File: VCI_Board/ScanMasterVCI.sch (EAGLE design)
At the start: 64 parts, among them IC1 XMEGA16A4A, IC2 LTC3631, IC3 LM317MDT, IC4 SN74AHCT1G04, IC5 SN74AHCT1G04, IC6 TL331, IC7 74AHCT1G32DBV, Q5 PZT3904, Q6 MMBT3904, Q7 MMBT4403, Q8 MMBT3904/SOT, U2 LM339MA, U3 MAX17502EATB+T, U4 MAX13444EASA+

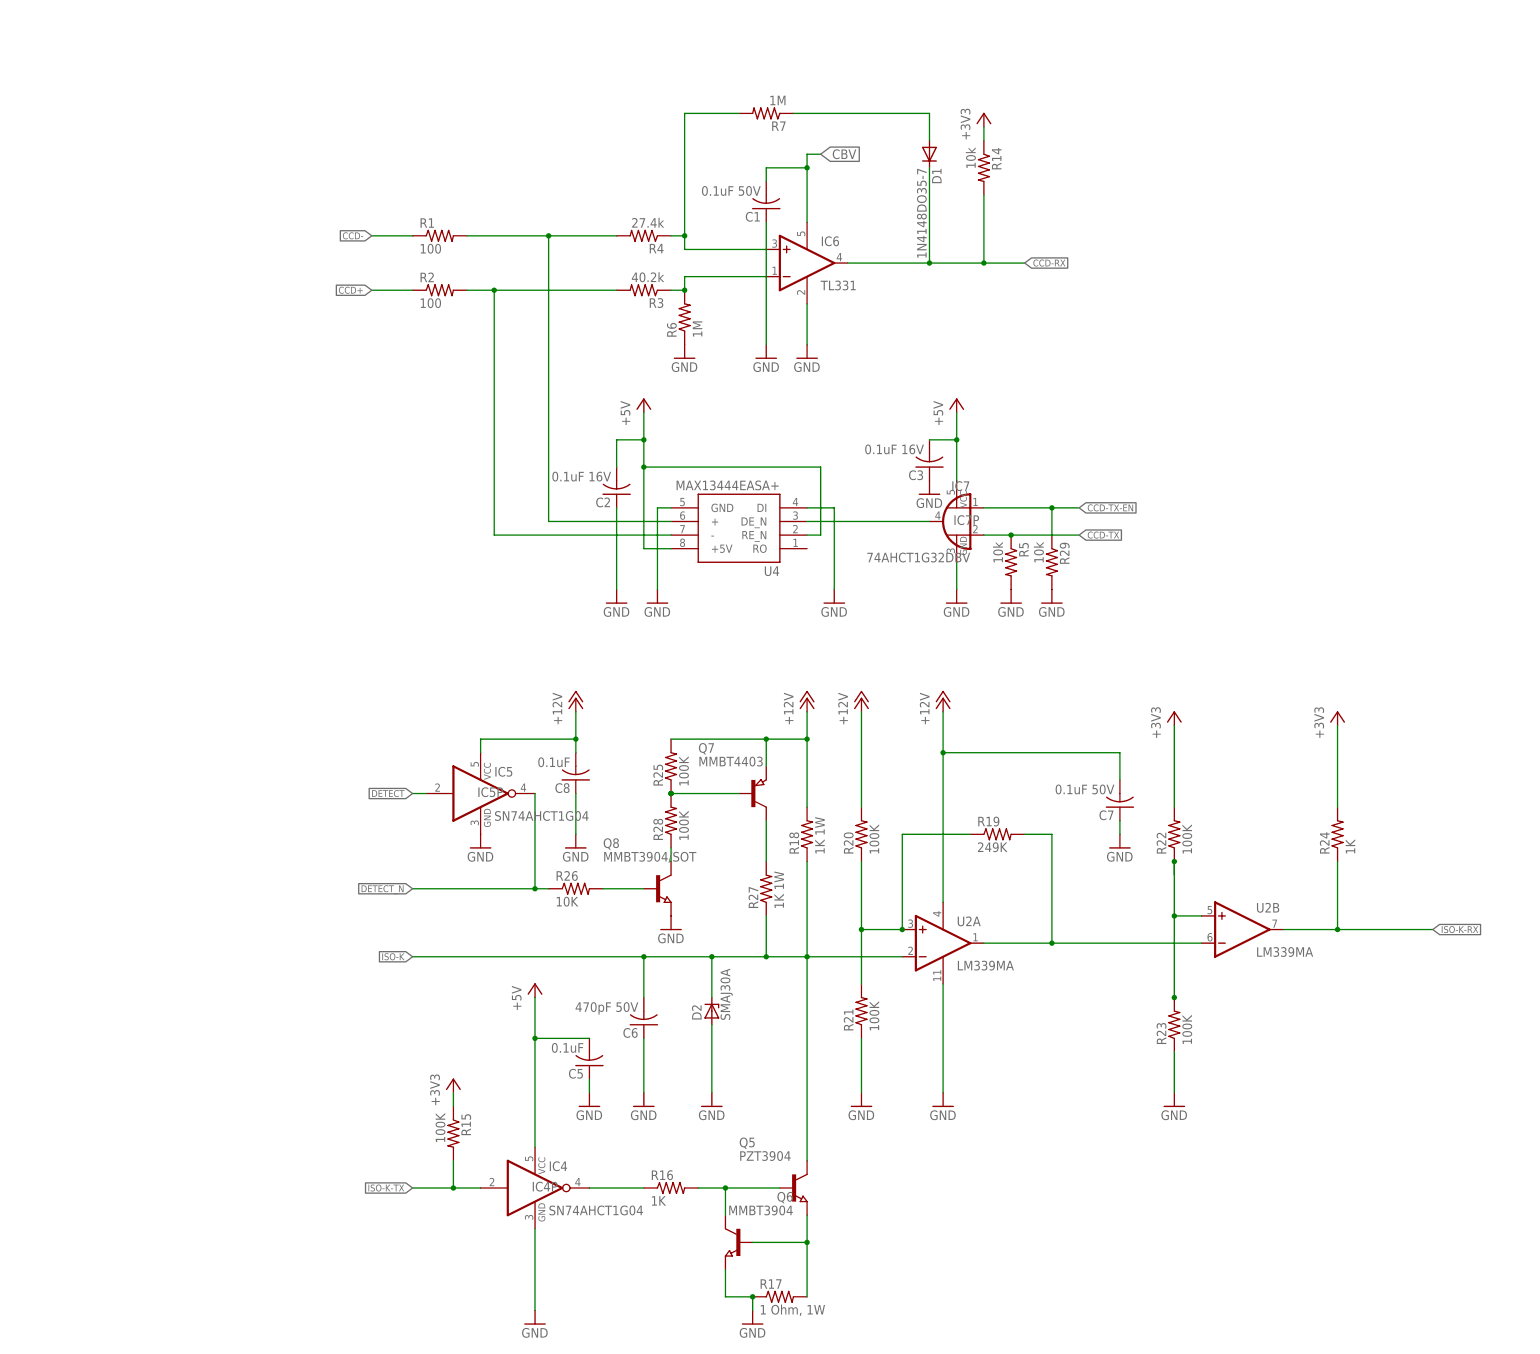
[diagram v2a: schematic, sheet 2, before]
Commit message: Designed a circuit for J1850VPW. Still some problems to be worked out, I think the input voltage is all wrong, but I'll need to put a scope on some J1850 ECU's to see exactly what my target "high" voltage should be.
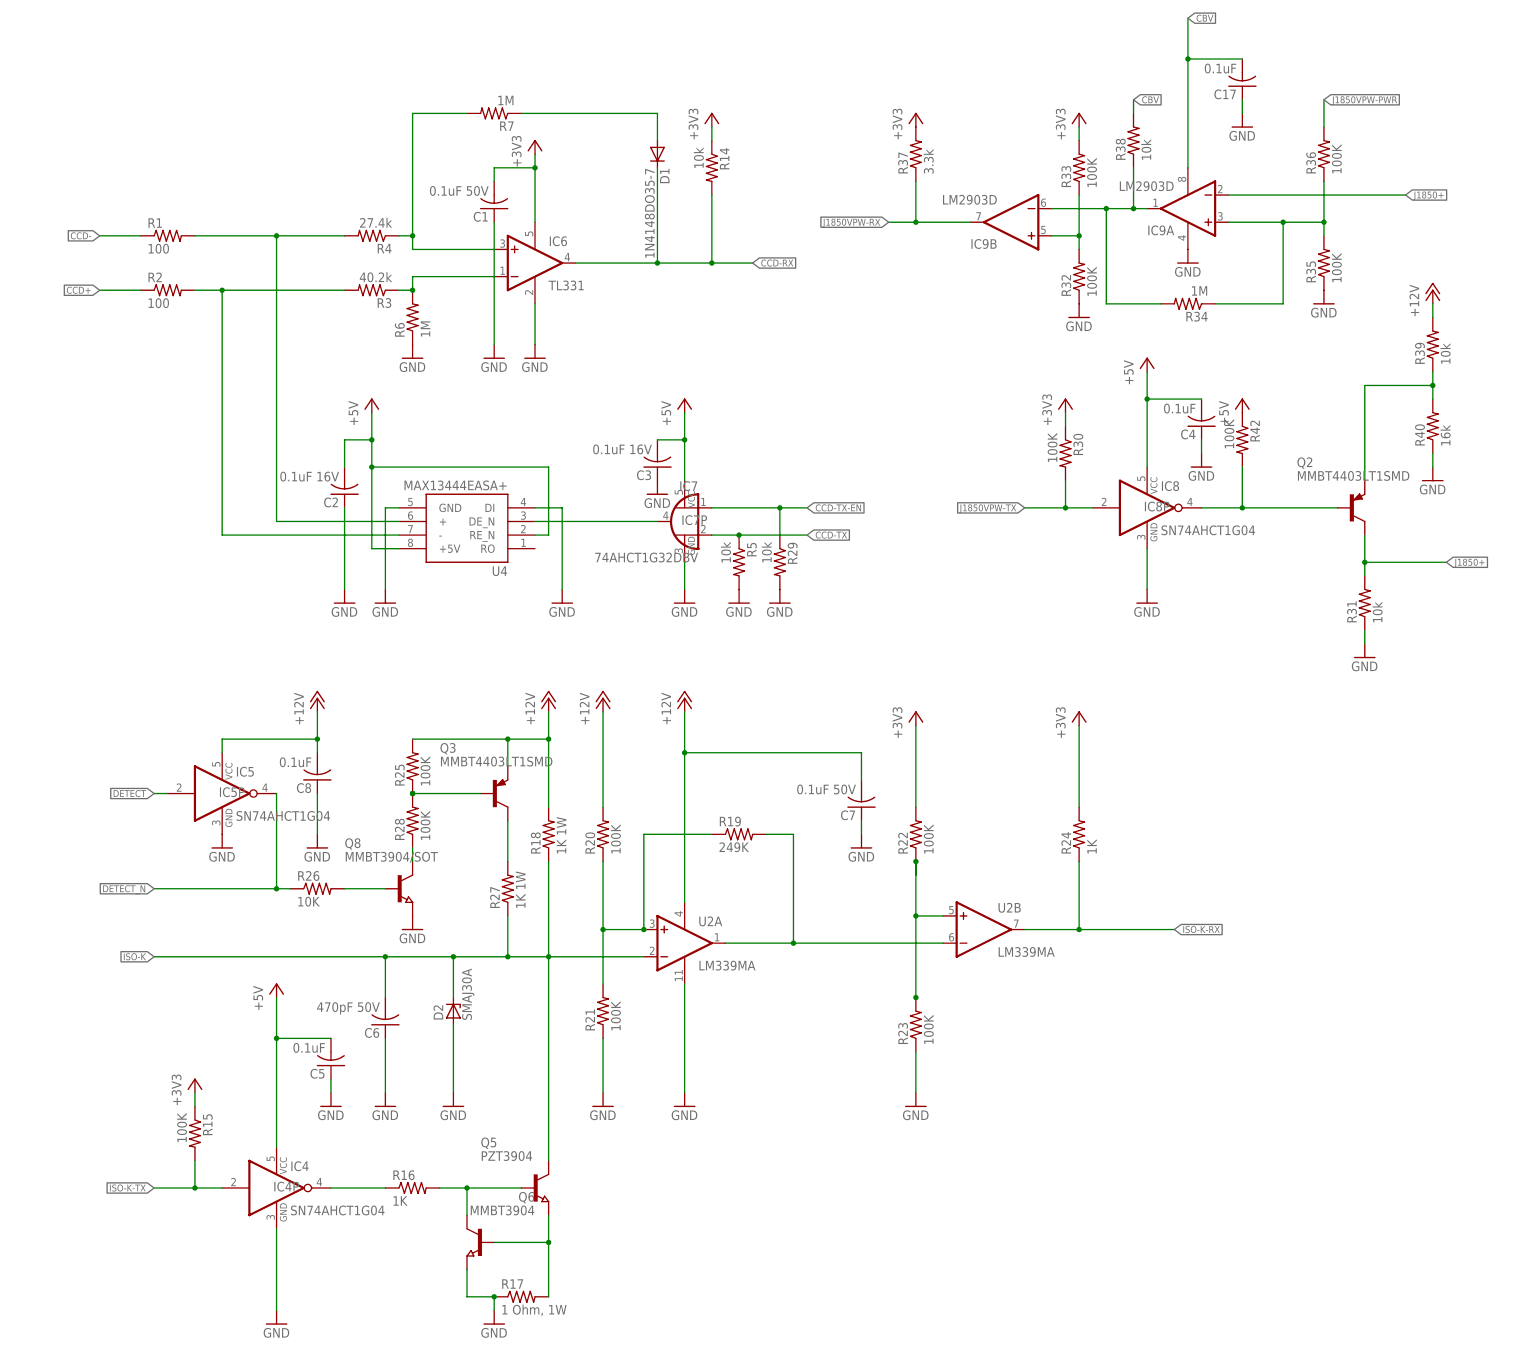
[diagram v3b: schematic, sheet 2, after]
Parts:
- removed Q7: MMBT4403, semicon-smd-ipc:PNP-TRANSISTOR_SOT23
- added C17, C4: 0.1uF, adafruit:C-USC0805
- added IC8: SN74AHCT1G04, 74xx-little-us:74AHC1G04DBV
- added IC9: LM2903D, linear:LM2903D
- added Q2, Q3: MMBT4403LT1SMD, transistor-pnp:MMBT4403LT1SMD
- added R30, R32, R33, R35, R36, R42: 100K, adafruit:R-US_R0805W
- added R31, R38, R39: 10k, adafruit:R-US_R0805W
- added R34: 1M, adafruit:R-US_R0805W
- added R37: 3.3k, adafruit:R-US_R0805W
- added R40: 16k, adafruit:R-US_R0805W
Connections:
- new net J1850+: IC9A.-IN, Q2.C, R31.2
- new net J1850VPW-RX: IC9B.OUT, R37.1
- new net J1850VPW-TX: IC8A.I, R30.2
- new net N$25: Q2.E, R39.1, R40.2
- new net N$27: IC9A.OUT, IC9B.-IN, R34.2, R38.1
- new net N$28: IC9B.+IN, R32.2, R33.1
- new net N$29: IC9A.+IN, R34.1, R35.2
- new net N$5: IC8A.O, Q2.B, R42.2
- net +12V: now also Q3.E, R39.2; no longer Q7.E
- net +3V3: now also C1.2, IC6.V+, R30.1, R33.2, R37.2
- net +5V: now also C4.2, IC8P.VCC, R42.1
- net CBV: now also C17.2, IC9P.V+, R38.2; no longer C1.2, IC6.V+
- net GND: now also C17.1, C4.1, IC8P.GND, IC9P.V-, R31.1, R32.1, R40.1
- net J1850VPW-PWR: now also R36.2
- net N$20: now also Q3.B; no longer Q7.B
- net N$23: now also Q3.C; no longer Q7.C
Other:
- moved on the sheet: C1, C2, C3, C5, C6, C7, C8, D1, D2, IC4, IC4P, IC5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

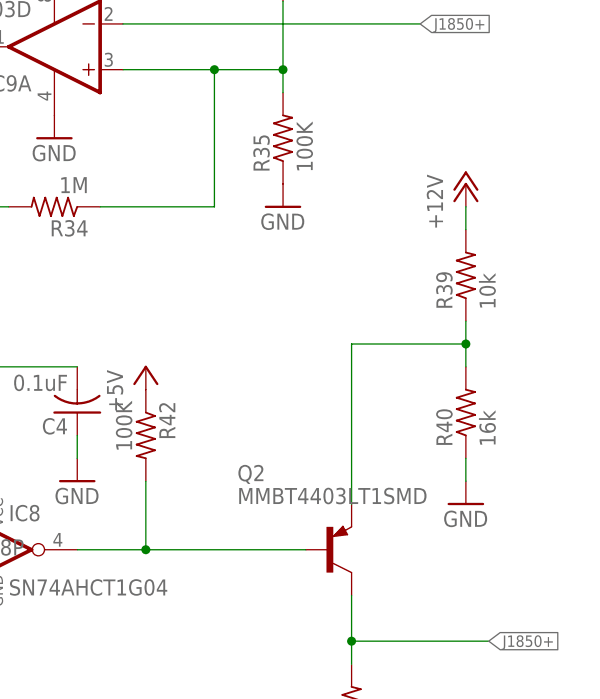
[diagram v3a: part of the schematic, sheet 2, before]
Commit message: Modified J1850 based on power findings
Scope shows ~7.3V for high signals. Unsure if current RX circuit is sufficient to drive that down to 3.3 volts. Still looking into more elegant solution.
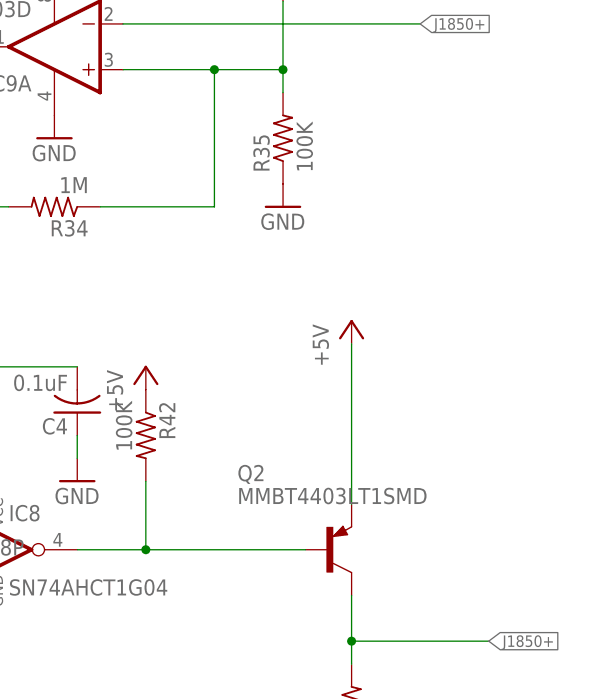
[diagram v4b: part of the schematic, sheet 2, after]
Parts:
- removed R39: 10k, adafruit:R-US_R0805W
- removed R40: 16k, adafruit:R-US_R0805W
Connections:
- removed net N$25: Q2.E, R39.1, R40.2
- net +12V: no longer R39.2
- net +5V: now also Q2.E
- net GND: no longer R40.1
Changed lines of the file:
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@@
 <part name="R31" library="adafruit" library_urn="urn:adsk.eagle:library:420" deviceset="R-US_" device="R0805W" value="10k"/>
 <part name="+3V10" library="supply1" library_urn="urn:adsk.eagle:library:371" deviceset="+3V3" device=""/>
-<part name="P+12" library="supply1" library_urn="urn:adsk.eagle:library:371" deviceset="+12V" device=""/>
-<part name="R39" library="adafruit" library_urn="urn:adsk.eagle:library:420" deviceset="R-US_" device="R0805W" value="10k"/>
-<part name="R40" library="adafruit" library_urn="urn:adsk.eagle:library:420" deviceset="R-US_" device="R0805W" value="16k"/>
-<part name="GND43" library="supply1" library_urn="urn:adsk.eagle:library:371" deviceset="GND" device=""/>
+<part name="P+12" library="supply1" library_urn="urn:adsk.eagle:library:371" deviceset="+5V" device=""/>
 </parts>
 <sheets>
@@
 <instance part="R31" gate="G$1" x="208.28" y="147.32" rot="R90"/>
 <instance part="+3V10" gate="G$1" x="53.34" y="233.68"/>
-<instance part="P+12" gate="1" x="220.98" y="205.74"/>
-<instance part="R39" gate="G$1" x="220.98" y="195.58" rot="R90"/>
-<instance part="R40" gate="G$1" x="220.98" y="180.34" rot="R90"/>
-<instance part="GND43" gate="1" x="220.98" y="170.18"/>
+<instance part="P+12" gate="1" x="208.28" y="190.5"/>
 </instances>
 <busses>
@@
 <pinref part="R31" gate="G$1" pin="1"/>
 <wire x1="208.28" y1="142.24" x2="208.28" y2="139.7" width="0.1524" layer="91"/>
-</segment>
-<segment>
-<pinref part="R40" gate="G$1" pin="1"/>
-<pinref part="GND43" gate="1" pin="GND"/>
-<wire x1="220.98" y1="175.26" x2="220.98" y2="172.72" width="0.1524" layer="91"/>
 </segment>
 </net>
@@
 <pinref part="R42" gate="G$1" pin="1"/>
 <pinref part="P+11" gate="1" pin="+5V"/>
+</segment>
+<segment>
+<pinref part="Q2" gate="G$1" pin="E"/>
+<wire x1="208.28" y1="187.96" x2="208.28" y2="170.18" width="0.1524" layer="91"/>
+<pinref part="P+12" gate="1" pin="+5V"/>
 </segment>
 </net>
@@
 <junction x="12.7" y="121.92"/>
 </segment>
-<segment>
-<pinref part="R39" gate="G$1" pin="2"/>
-<pinref part="P+12" gate="1" pin="+12V"/>
-<wire x1="220.98" y1="200.66" x2="220.98" y2="203.2" width="0.1524" layer="91"/>
-</segment>
 </net>
 <net name="N$17" class="0">
@@
 </segment>
 </net>
-<net name="N$25" class="0">
-<segment>
-<pinref part="Q2" gate="G$1" pin="E"/>
-<wire x1="208.28" y1="187.96" x2="208.28" y2="170.18" width="0.1524" layer="91"/>
-<pinref part="R39" gate="G$1" pin="1"/>
-<wire x1="220.98" y1="190.5" x2="220.98" y2="187.96" width="0.1524" layer="91"/>
-<pinref part="R40" gate="G$1" pin="2"/>
-<wire x1="220.98" y1="187.96" x2="220.98" y2="185.42" width="0.1524" layer="91"/>
-<wire x1="208.28" y1="187.96" x2="220.98" y2="187.96" width="0.1524" layer="91"/>
-<junction x="220.98" y="187.96"/>
-</segment>
-</net>

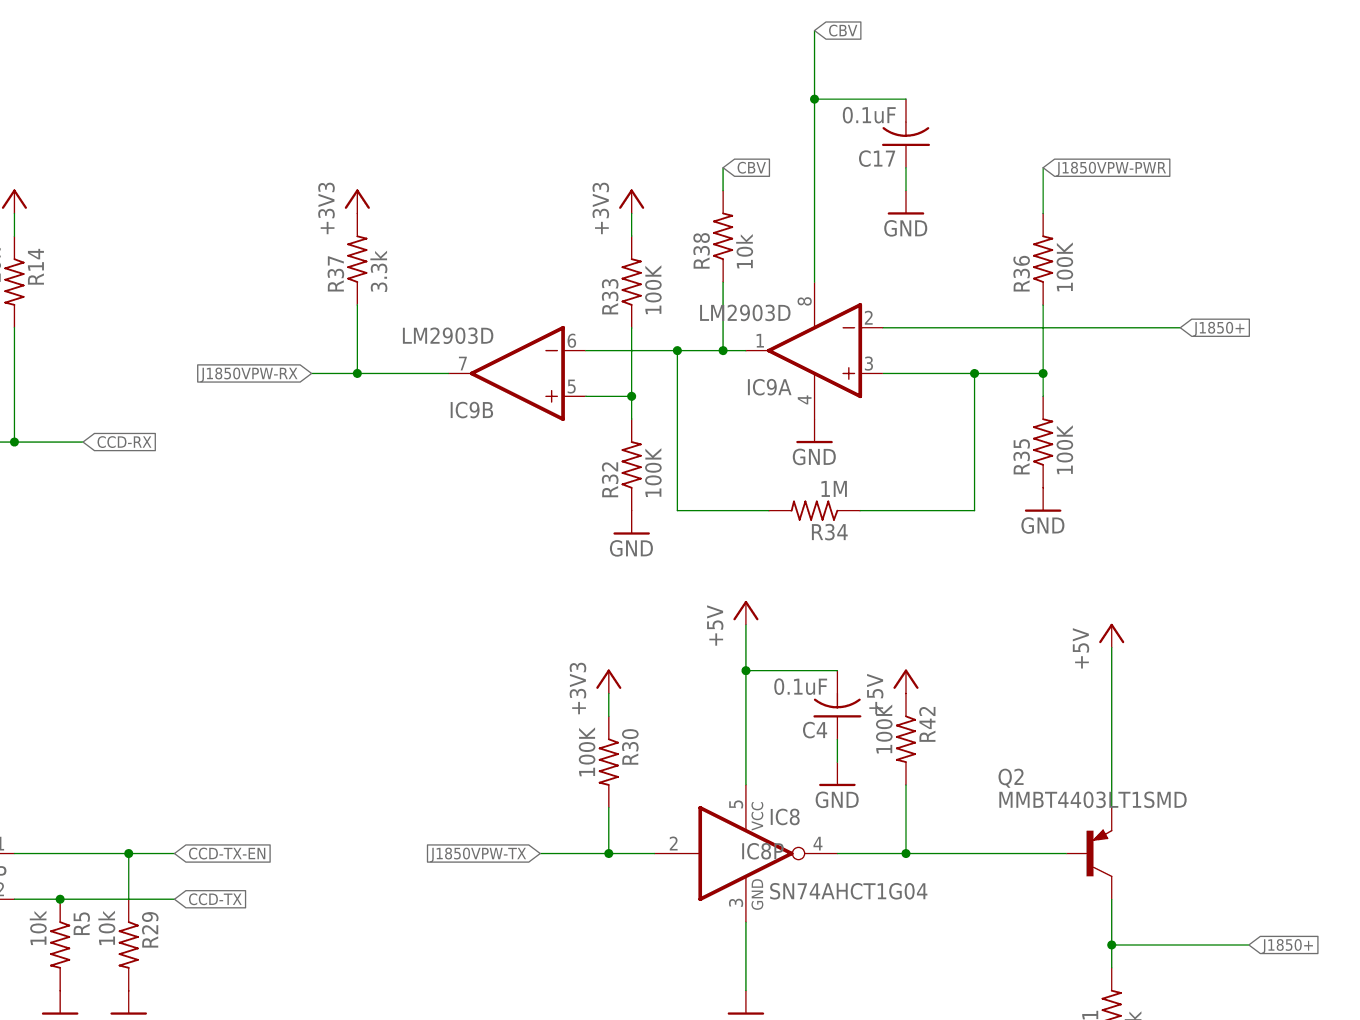
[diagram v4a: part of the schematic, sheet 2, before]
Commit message: Re-worked J1850-RX. Removed dependency on the specialty power circuit. We'll just use 5V to drive VPW high.
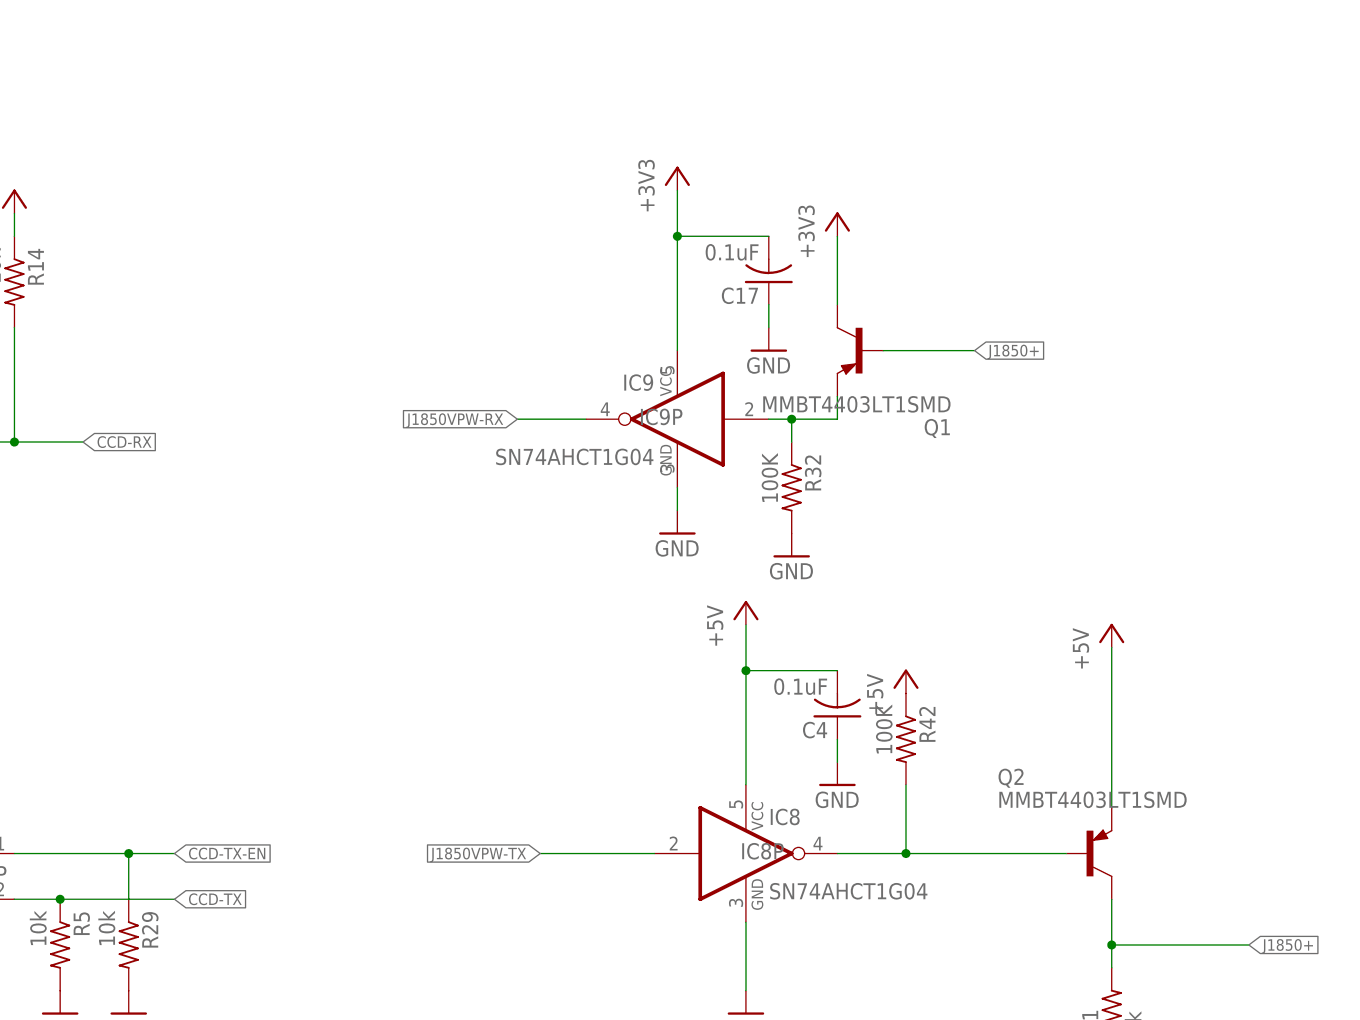
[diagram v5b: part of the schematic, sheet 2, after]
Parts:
- removed R30, R33, R35, R36: 100K, adafruit:R-US_R0805W
- removed R34: 1M, adafruit:R-US_R0805W
- removed R37: 3.3k, adafruit:R-US_R0805W
- removed R38: 10k, adafruit:R-US_R0805W
- added Q1: MMBT4403LT1SMD, transistor-pnp:MMBT4403LT1SMD
- IC9: value LM2903D -> SN74AHCT1G04; device linear:LM2903D -> 74xx-little-us:74AHC1G04DBV
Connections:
- removed net N$27: IC9A.OUT, IC9B.-IN, R34.2, R38.1
- removed net N$28: IC9B.+IN, R32.2, R33.1
- removed net N$29: IC9A.+IN, R34.1, R35.2
- new net N$26: IC9A.I, Q1.E, R32.1
- net +3V3: now also C17.2, IC9P.VCC, Q1.C; no longer R30.1, R33.2, R37.2
- net CBV: no longer C17.2, IC9P.V+, R38.2
- net GND: now also IC9P.GND, R32.2; no longer IC9P.V-, R32.1
- net J1850+: now also Q1.B; no longer IC9A.-IN
- net J1850VPW-PWR: no longer R36.2
- net J1850VPW-RX: now also IC9A.O; no longer IC9B.OUT, R37.1
- net J1850VPW-TX: no longer R30.2
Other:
- moved on the sheet: C17, R32
